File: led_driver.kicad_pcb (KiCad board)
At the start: 2 copper layers, 74.9 x 64.8 mm, 27 parts, among them P1 PIN, T1 MOSFET, T2 MOSFET, T3 MOSFET, T4 MOSFET, T5 MOSFET, T6 MOSFET, U1 Teensy_3.1

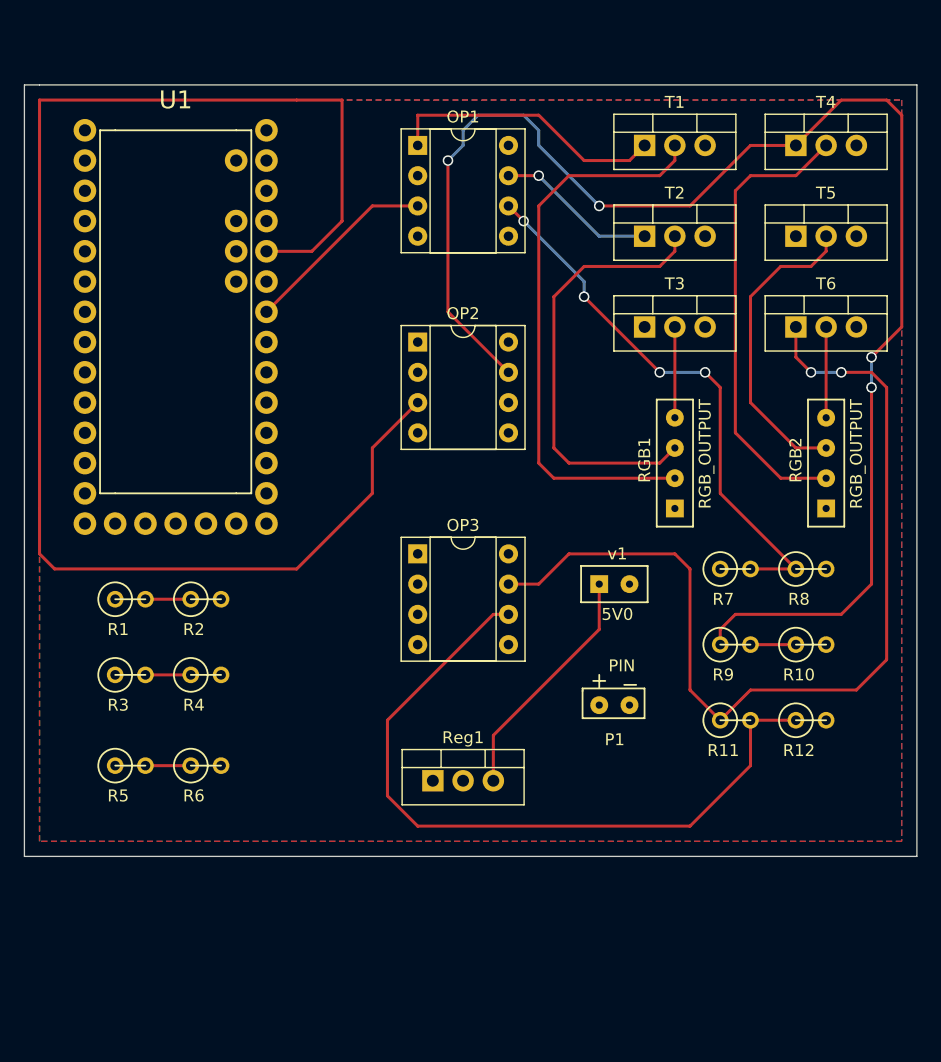
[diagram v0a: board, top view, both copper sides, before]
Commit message: added schematic print. Produced GERBER files (manufacturing drawings). Slight rewiring to give larger passage ways for higher current flow
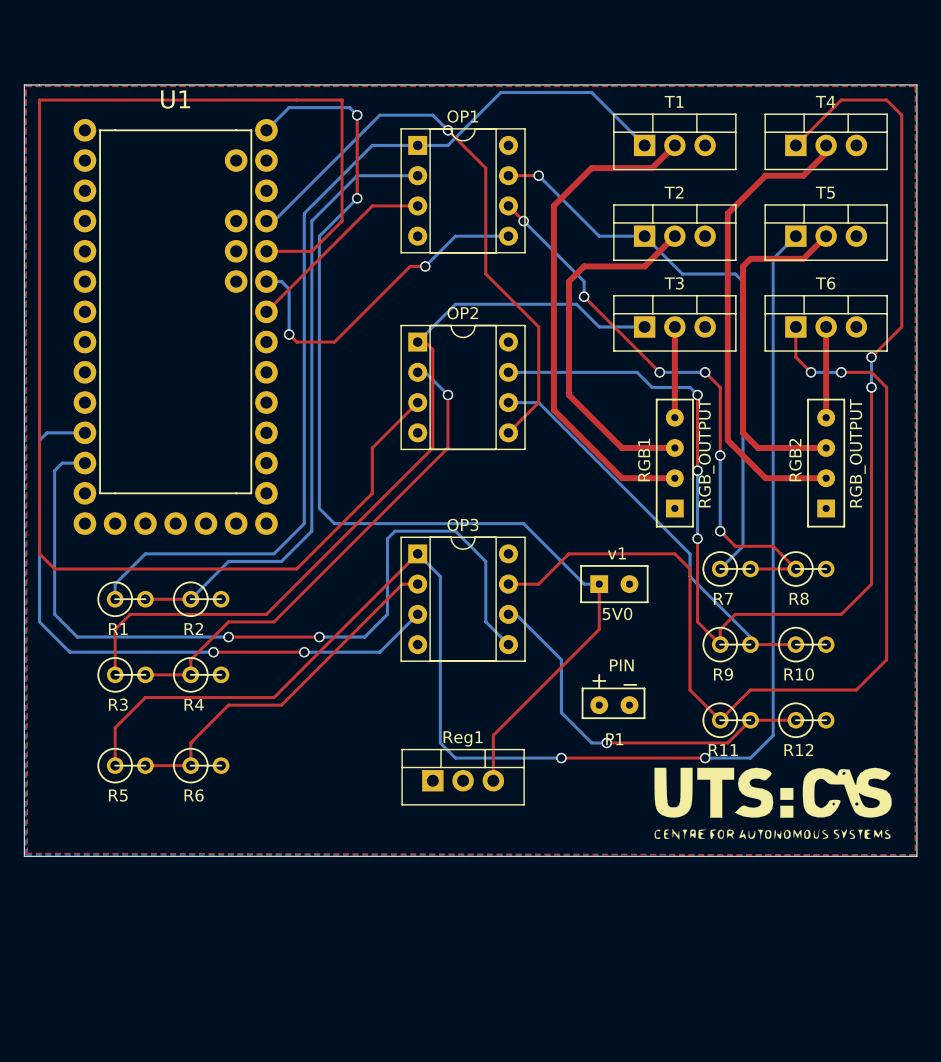
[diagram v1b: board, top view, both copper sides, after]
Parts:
- added G***: LOGO, images:logo, F.Cu at (228.0, 174.6)
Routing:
- net ING2: track 0.00 -> 123.2 mm, vias 0 -> 2
- net Net-(Reg1-Pad3): track 20.2 -> 89.3 mm, vias 0 -> 2
- net B2: track 0.00 -> 68.1 mm, vias 0 -> 2
- net INB1: track 0.00 -> 67.7 mm
- net INR1: track 23.7 -> 79.9 mm
- net G2: track 0.00 -> 53.4 mm, vias 0 -> 2
- net R2: track 0.00 -> 49.1 mm, vias 0 -> 1
- net Net-(OP1-Pad2): track 3.81 -> 52.8 mm
- net Net-(OP2-Pad2): track 3.81 -> 41.8 mm, vias 0 -> 1
- net ING1: track 13.5 -> 48.3 mm
- net Net-(OP2-Pad6): track 3.81 -> 34.0 mm
- net Net-(OP3-Pad6): track 61.4 -> 32.0 mm, vias 0 -> 1
- net G1: track 0.00 -> 28.3 mm, vias 0 -> 2
- net Net-(OP3-Pad2): track 3.81 -> 30.3 mm
- net INR2: track 124.4 -> 107.5 mm, vias 4 -> 5
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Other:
- net class colour_out added: clearance 0.254, trace_width 0.5, via_dia 0.889, via_drill 0.635

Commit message: added DC jack, added 3d models for the RGB connectors and opamps
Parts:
- added pnglogo: , images:logov2, F.Cu at (182.0, 173.1)
- P1: footprint PIN:PIN -> Connectors:BARREL_JACK
- moved P1 37.5 mm to (179.1, 181.6)
- moved G*** 10.8 mm to (229.6, 185.3)
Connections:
- U1 pad 0: Net-(U1-Pad0) -> (no net)
- U1 pad 1: Net-(U1-Pad1) -> (no net)
- U1 pad 11: Net-(U1-Pad11) -> (no net)
- U1 pad 12: Net-(U1-Pad12) -> (no net)
- U1 pad 13: Net-(U1-Pad13) -> (no net)
- U1 pad 14: Net-(U1-Pad14) -> (no net)
- U1 pad 15: Net-(U1-Pad15) -> (no net)
- U1 pad 16: Net-(U1-Pad16) -> (no net)
- U1 pad 17: Net-(U1-Pad17) -> (no net)
- U1 pad 18: Net-(U1-Pad18) -> (no net)
- U1 pad 19: Net-(U1-Pad19) -> (no net)
- U1 pad 2: Net-(U1-Pad2) -> (no net)
- U1 pad 24: Net-(U1-Pad24) -> (no net)
- U1 pad 25: Net-(U1-Pad25) -> (no net)
- U1 pad 28: Net-(U1-Pad28) -> (no net)
- U1 pad 29: Net-(U1-Pad29) -> (no net)
- U1 pad 3: Net-(U1-Pad3) -> (no net)
- U1 pad 31: Net-(U1-Pad31) -> (no net)
- U1 pad 32: Net-(U1-Pad32) -> (no net)
- U1 pad 33: Net-(U1-Pad33) -> (no net)
- U1 pad 34: Net-(U1-Pad34) -> (no net)
- U1 pad 35: Net-(U1-Pad35) -> (no net)
- U1 pad 36: Net-(U1-Pad36) -> (no net)
- U1 pad 4: Net-(U1-Pad4) -> (no net)
- U1 pad 5: Net-(U1-Pad5) -> (no net)
- U1 pad 6: Net-(U1-Pad6) -> (no net)
- U1 pad 7: Net-(U1-Pad7) -> (no net)
- U1 pad 8: Net-(U1-Pad8) -> (no net)
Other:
- board size 74.9 x 64.8 mm -> 74.9 x 74.9 mm
- board text added: "12V"
- board text added: "5V"
- board text added: "GND"

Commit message: fixed DC barrel jack slot issue
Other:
- board text added: "RGB LED Strip Driver Rev 1.0 Author: Denis Draca (MMD 2017 Autumn)"
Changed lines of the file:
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@@
-(kicad_pcb (version 4) (host pcbnew 4.0.6)
+(kicad_pcb (version 4) (host pcbnew 4.0.6-e0-6349~53~ubuntu14.04.1)
   (general
     (links 63)
@@
     (area 164.790999 114.191 240.080001 189.280001)
     (thickness 1.6)
-    (drawings 11)
+    (drawings 12)
     (tracks 250)
     (zones 0)
@@
     (34 B.Paste user)
     (35 F.Paste user)
-    (36 B.SilkS user hide)
+    (36 B.SilkS user)
     (37 F.SilkS user)
     (38 B.Mask user hide)
@@
     (mod_text_size 1 1)
     (mod_text_width 0.15)
-    (pad_size 1.5 1.5)
-    (pad_drill 0.6)
+    (pad_size 4 4)
+    (pad_drill 3)
     (pad_to_mask_clearance 0)
     (aux_axis_origin 0 0)
@@
       (rotate (xyz 0 0 -90))
     )
+    (model ../../../../../home/denis/Desktop/led_pcb/3d_footprints/dip8wrl.wrl
+      (at (xyz 0.15 -0.15 0))
+      (scale (xyz 0.3937 0.3937 0.3937))
+      (rotate (xyz 0 0 -90))
+    )
   )
   (module Housings_DIP:DIP-8_W7.62mm_Socket (layer F.Cu)
@@
       (rotate (xyz 0 0 -90))
     )
+    (model ../../../../../home/denis/Desktop/led_pcb/3d_footprints/dip8wrl.wrl
+      (at (xyz 0.15 -0.15 0))
+      (scale (xyz 0.3937 0.3937 0.3937))
+      (rotate (xyz 0 0 -90))
+    )
   )
   (module Housings_DIP:DIP-8_W7.62mm_Socket (layer F.Cu)
@@
       (rotate (xyz 0 0 -90))
     )
+    (model /home/denis/Desktop/led_pcb/3d_footprints/dip8wrl.wrl
+      (at (xyz 0.15 -0.15 0))
+      (scale (xyz 0.3937 0.3937 0.3937))
+      (rotate (xyz 0 0 -90))
+    )
   )
   (module Discret:R1 (layer F.Cu)
@@
       (rotate (xyz -90 0 0))
     )
+    (model ../../../../../home/denis/Desktop/led_pcb/3d_footprints/4pinMolex.wrl
+      (at (xyz 0.15 0 0))
+      (scale (xyz 0.3937 0.3937 0.3937))
+      (rotate (xyz -90 0 0))
+    )
   )
   (module rgbOUT:rgbOUT (layer F.Cu)
@@
       (rotate (xyz -90 0 0))
     )
+    (model ../../../../../home/denis/Desktop/led_pcb/3d_footprints/4pinMolex.wrl
+      (at (xyz 0.15 0 0))
+      (scale (xyz 0.3937 0.3937 0.3937))
+      (rotate (xyz -90 0 0))
+    )
   )
   (module TO_SOT_Packages_THT:TO-220_Vertical (layer F.Cu)
@@
       (rotate (xyz 0 0 90))
     )
+    (model ../../../../../home/denis/Desktop/led_pcb/3d_footprints/teensy.wrl
+      (at (xyz 0.55 0.3 0.05))
+      (scale (xyz 0.3937 0.3937 0.3937))
+      (rotate (xyz 0 0 90))
+    )
   )
   (module 5vIN:5vIN (layer F.Cu)
@@
       (rotate (xyz -90 0 0))
     )
+    (model ../../../../../home/denis/Desktop/led_pcb/3d_footprints/2pinMolex.wrl
+      (at (xyz 0.05 0 0))
+      (scale (xyz 0.3937 0.3937 0.3937))
+      (rotate (xyz -90 0 0))
+    )
   )
   (module Connectors:BARREL_JACK (layer F.Cu)
@@
     (fp_line (start 0.8 4.5) (end 0.8 -4.5) (layer F.Fab) (width 0.1))
     (fp_line (start 0.8 -4.5) (end -13.7 -4.5) (layer F.Fab) (width 0.1))
-    (pad 1 thru_hole rect (at 0 0) (size 3.5 3.5) (drill oval 1 3) (layers *.Cu *.Mask)
+    (pad 1 thru_hole rect (at 0 0) (size 4 4) (drill 3) (layers *.Cu *.Mask)
       (net 8 VCC))
-    (pad 2 thru_hole rect (at -6 0) (size 3.5 3.5) (drill oval 1 3) (layers *.Cu *.Mask)
+    (pad 2 thru_hole rect (at -6 0) (size 4 4) (drill 3) (layers *.Cu *.Mask)
       (net 7 GND))
-    (pad 3 thru_hole rect (at -3 4.7) (size 3.5 3.5) (drill oval 3 1) (layers *.Cu *.Mask))
+    (pad 3 thru_hole rect (at -3 4.7) (size 4 4) (drill 3) (layers *.Cu *.Mask))
     (model "../../../../../../Users/Denis Draca/Desktop/led_circuit/3d_footprints/AB2_PB_2MM_JACK_PTH.wrl"
       (at (xyz -0.55 0 0))
@@
       (rotate (xyz 0 0 90))
     )
+    (model ../../../../../home/denis/Desktop/led_pcb/3d_footprints/AB2_PB_2MM_JACK_PTH.wrl
+      (at (xyz -0.55 0 0))
+      (scale (xyz 0.3937 0.3937 0.3937))
+      (rotate (xyz 0 0 90))
+    )
   )
   (module images:logo (layer F.Cu)
@@
       (xy 5.9 14.9)) (layer F.SilkS) (width 0.01))
   )
+  (gr_text "RGB LED Strip Driver\nRev 1.0\nAuthor: Denis Draca (MMD 2017 Autumn)" (at 238.76 184.404) (layer B.SilkS)
+    (effects (font (size 1.5 1.5) (thickness 0.3)) (justify left mirror))
+  )
   (gr_text GND (at 219.075 156.21) (layer F.SilkS)

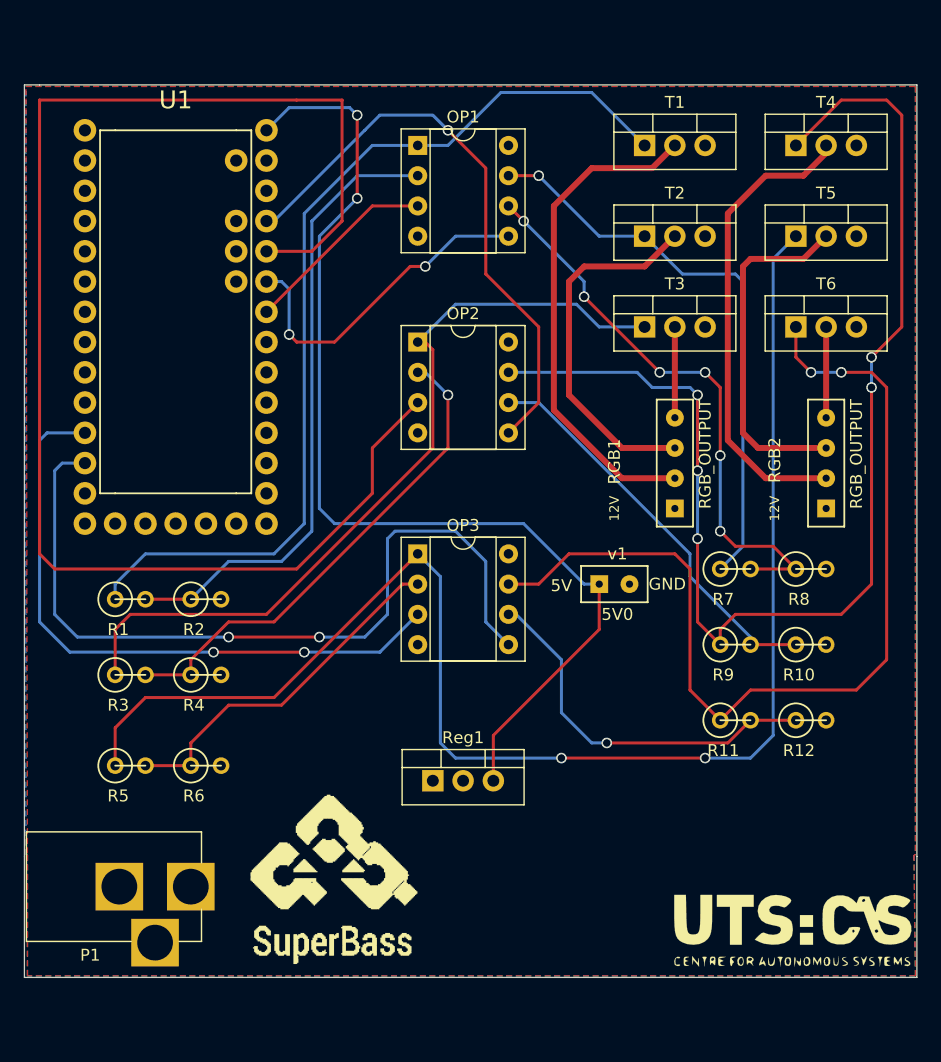
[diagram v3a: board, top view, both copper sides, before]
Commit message: fixed hole size for headers
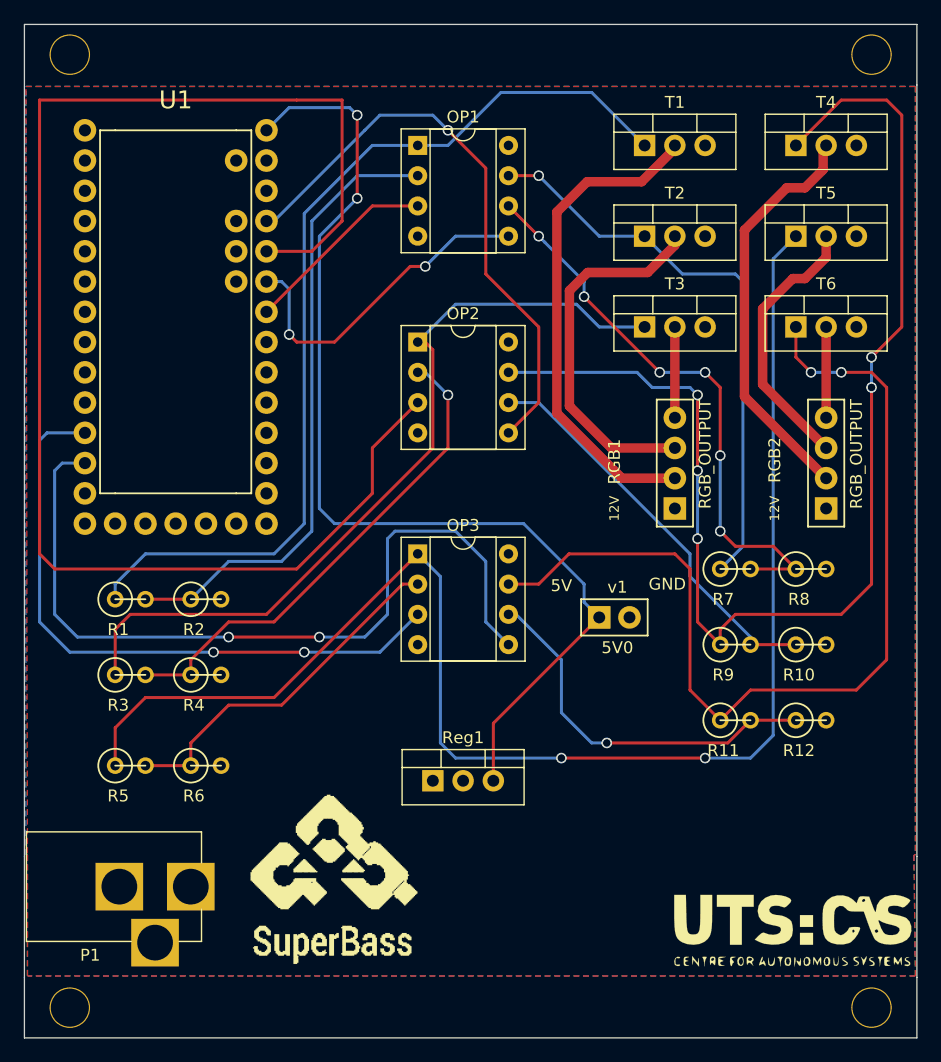
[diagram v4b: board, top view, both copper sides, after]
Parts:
- added REF**: MountingHole_3.2mm_M3_DIN965, Mounting_Holes:MountingHole_3.2mm_M3_DIN965, F.Cu at (168.9, 111.8)
- added REF**: MountingHole_3.2mm_M3_DIN965, Mounting_Holes:MountingHole_3.2mm_M3_DIN965, F.Cu at (236.2, 111.8)
- added REF**: MountingHole_3.2mm_M3_DIN965, Mounting_Holes:MountingHole_3.2mm_M3_DIN965, F.Cu at (168.9, 191.8)
- added REF**: MountingHole_3.2mm_M3_DIN965, Mounting_Holes:MountingHole_3.2mm_M3_DIN965, F.Cu at (236.2, 191.8)
- moved v1 2.79 mm to (213.4, 159.0)
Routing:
- net OUTG2: track 29.5 -> 22.8 mm
- net OUTR2: track 39.6 -> 35.1 mm
- net OUTR1: track 41.9 -> 45.9 mm
- net Net-(Reg1-Pad3): track 89.3 -> 88.6 mm
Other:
- board size 74.9 x 74.9 mm -> 74.9 x 85.1 mm
- net class colour_out: trace_width 0.5 -> 0.8
